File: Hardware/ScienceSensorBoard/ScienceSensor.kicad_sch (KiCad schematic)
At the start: 94 parts, among them J1 Conn_02x03_Counter_Clockwise, J2 RJ45_LED_Shielded, Q1 SI4156DY, Q10 BSS138, Q11 SI4156DY, Q2 SI4156DY, Q3 SI4156DY, Q4 BSS138, Q5 BSS138, Q6 BSS138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

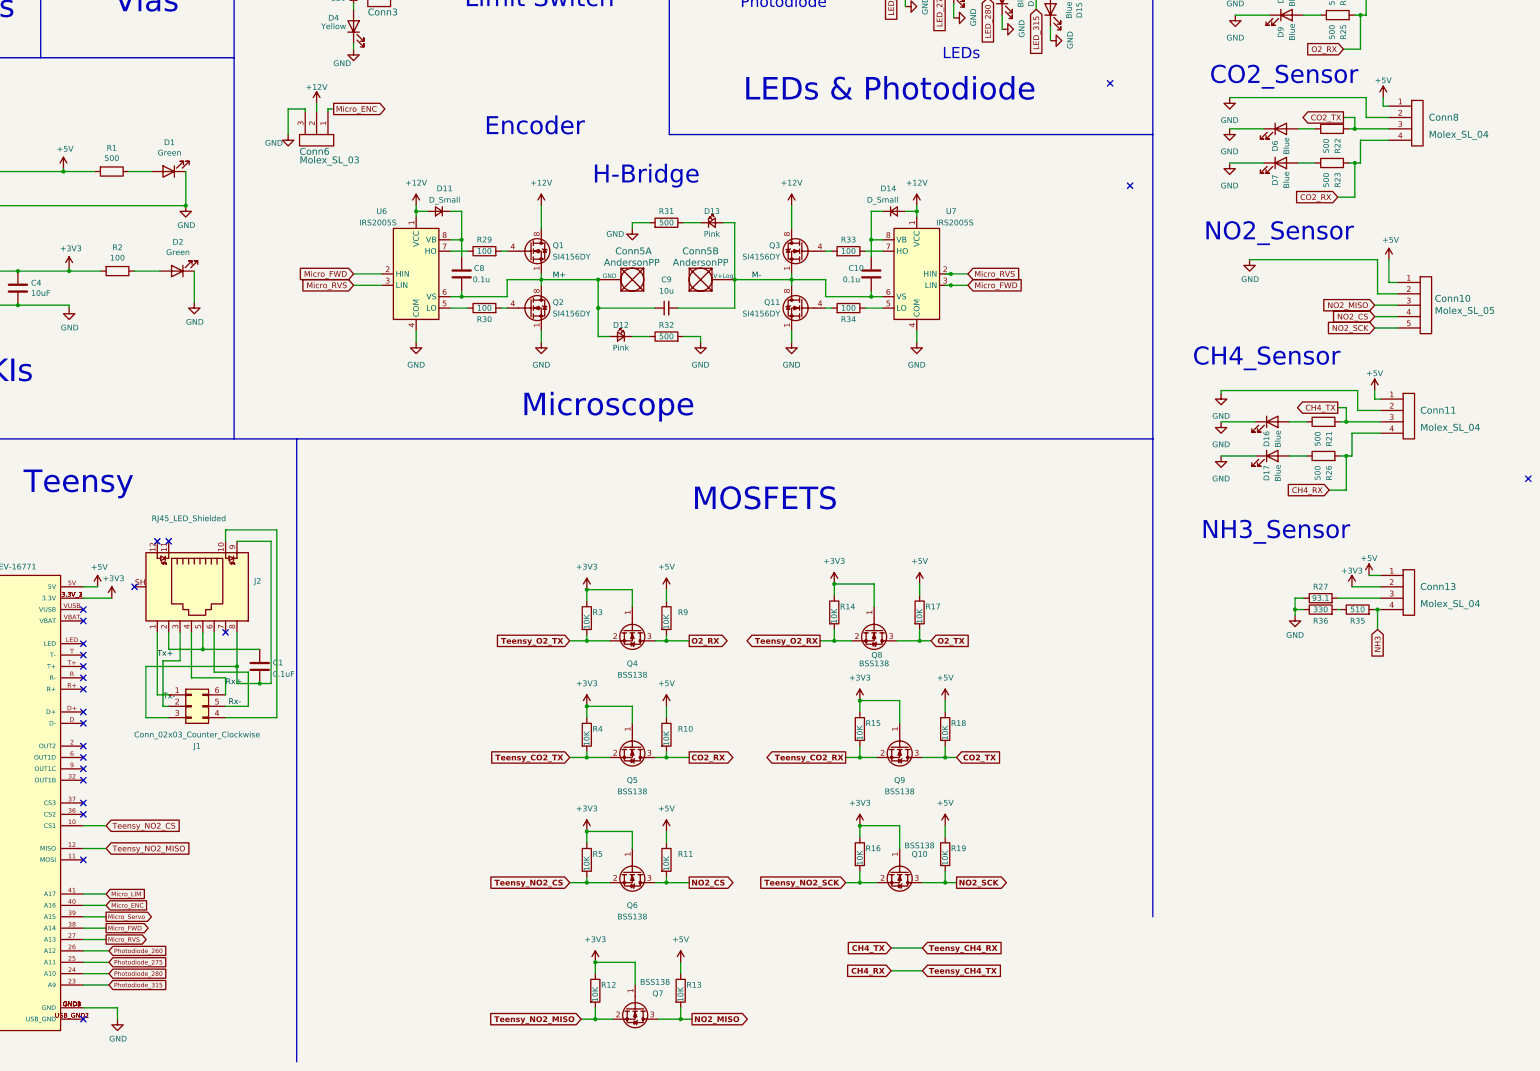
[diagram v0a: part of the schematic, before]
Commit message: ERC fixes
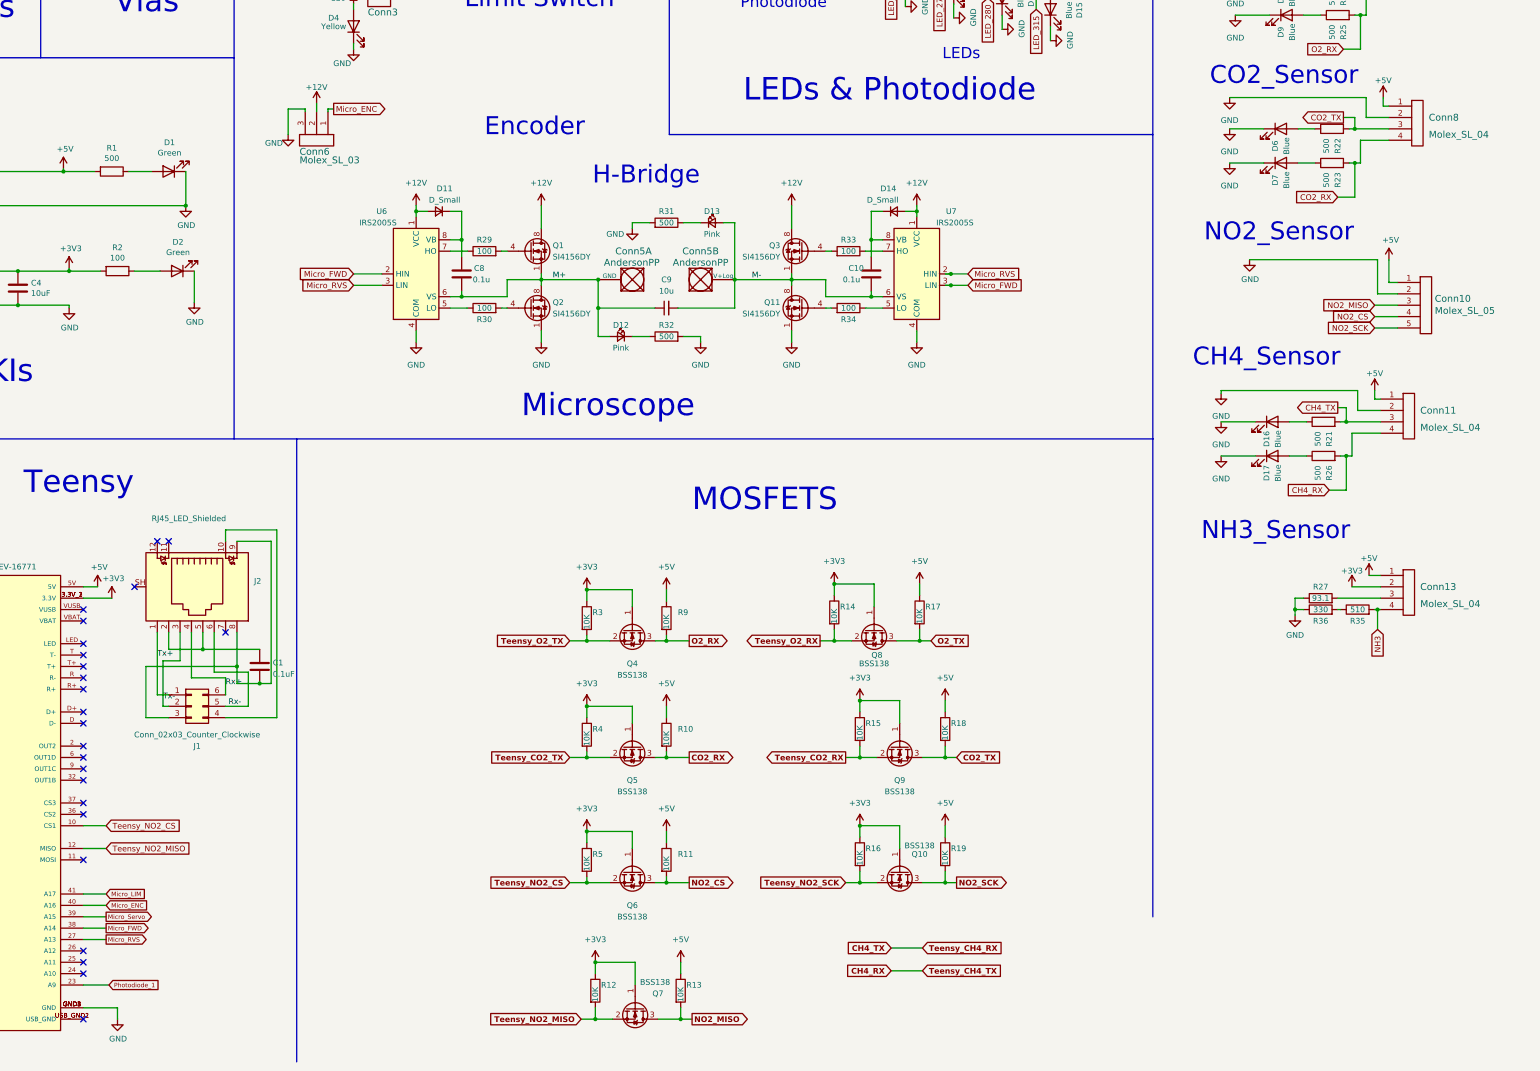
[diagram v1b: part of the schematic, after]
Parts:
- Conn10: footprint MRDT_Connectors:MOLEX_SL_05_Horizontal -> MRDT_Connectors:MOLEX_SL_05_Vertical
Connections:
- net Photodiode_315 is gone; now on net Photodiode_1: U3.23 (A9)
- net Photodiode_260: no longer names the net of U3.26 (A12)
- net Photodiode_275: no longer names the net of U3.25 (A11)
- net Photodiode_280: no longer names the net of U3.24 (A10)
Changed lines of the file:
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@@
   (no_connect (at 37.465 240.03))
   (no_connect (at 78.105 229.87))
+  (no_connect (at 78.105 260.35))
+  (no_connect (at 78.105 262.89))
+  (no_connect (at 78.105 265.43))
   (no_connect (at 94.615 168.91))
   (no_connect (at 97.155 168.91))
@@
   (no_connect (at 37.465 257.81))
   (no_connect (at 37.465 260.35))
-  (no_connect (at 400.685 154.94))
-  (no_connect (at 311.785 89.535))
-  (no_connect (at 307.34 66.675))
   (no_connect (at 297.18 24.765))
   (no_connect (at 37.465 234.95))
@@
     (stroke (width 0) (type default) (color 0 0 0 0))
   )
-  (wire (pts (xy 83.82 260.35) (xy 78.105 260.35))
-    (stroke (width 0) (type default) (color 0 0 0 0))
-  )
   (wire (pts (xy 172.72 110.49) (xy 180.34 110.49))
     (stroke (width 0) (type default) (color 0 0 0 0))
@@
     (stroke (width 0) (type default) (color 0 0 0 0))
   )
-  (wire (pts (xy 83.82 262.89) (xy 78.105 262.89))
-    (stroke (width 0) (type default) (color 0 0 0 0))
-  )
   (wire (pts (xy 33.655 212.09) (xy 37.465 212.09))
     (stroke (width 0) (type default) (color 0 0 0 0))
@@
     (stroke (width 0) (type default) (color 0 0 0 0))
   )
-  (wire (pts (xy 83.82 265.43) (xy 78.105 265.43))
-    (stroke (width 0) (type default) (color 0 0 0 0))
-  )
   (wire (pts (xy 270.51 204.47) (xy 270.51 207.01))
     (stroke (width 0) (type default) (color 0 0 0 0))
@@
     )
   )
-  (global_label "Photodiode_315" (shape input) (at 83.82 267.97 0) (fields_autoplaced)
+  (global_label "Photodiode_1" (shape input) (at 83.82 267.97 0) (fields_autoplaced)
     (effects (font (size 0.9906 0.9906)) (justify left))
-    (property "Intersheet References" "${INTERSHEET_REFS}" (id 0) (at 97.4727 267.9081 0)
+    (property "Intersheet References" "${INTERSHEET_REFS}" (id 0) (at 95.5859 267.9081 0)
       (effects (font (size 0.9906 0.9906)) (justify left) hide)
     )
@@
     )
   )
-  (global_label "Photodiode_280" (shape input) (at 83.82 265.43 0) (fields_autoplaced)
-    (effects (font (size 0.9906 0.9906)) (justify left))
-    (property "Intersheet References" "${INTERSHEET_REFS}" (id 0) (at 97.4727 265.3681 0)
-      (effects (font (size 0.9906 0.9906)) (justify left) hide)
-    )
-  )
   (global_label "Photodiode_1" (shape output) (at 226.06 42.545 180) (fields_autoplaced)
     (effects (font (size 1.27 1.27)) (justify right))
@@
     )
   )
-  (global_label "Photodiode_275" (shape input) (at 83.82 262.89 0) (fields_autoplaced)
-    (effects (font (size 0.9906 0.9906)) (justify left))
-    (property "Intersheet References" "${INTERSHEET_REFS}" (id 0) (at 97.4727 262.8281 0)
-      (effects (font (size 0.9906 0.9906)) (justify left) hide)
-    )
-  )
   (global_label "Micro_FWD" (shape output) (at 83.185 255.27 0) (fields_autoplaced)
     (effects (font (size 1 1)) (justify left))
@@
     )
   )
-  (global_label "Photodiode_260" (shape input) (at 83.82 260.35 0) (fields_autoplaced)
-    (effects (font (size 0.9906 0.9906)) (justify left))
-    (property "Intersheet References" "${INTERSHEET_REFS}" (id 0) (at 97.4727 260.2881 0)
-      (effects (font (size 0.9906 0.9906)) (justify left) hide)
-    )
-  )
   (global_label "NO2_MISO" (shape output) (at 213.995 275.59 0) (fields_autoplaced)
     (effects (font (size 1.27 1.27) bold) (justify left))
@@
       (effects (font (size 1.524 1.524)) (justify left))
     )
-    (property "Footprint" "MRDT_Connectors:MOLEX_SL_05_Horizontal" (id 2) (at 376.555 122.555 0)
+    (property "Footprint" "MRDT_Connectors:MOLEX_SL_05_Vertical" (id 2) (at 376.555 122.555 0)
       (effects (font (size 1.524 1.524)) hide)
     )
@@
     )
     (path "/c5c8c731-d752-4329-b481-00d81fff6183"
-      (reference "Conn10") (unit 1) (value "Molex_SL_05") (footprint "MRDT_Connectors:MOLEX_SL_05_Horizontal")
+      (reference "Conn10") (unit 1) (value "Molex_SL_05") (footprint "MRDT_Connectors:MOLEX_SL_05_Vertical")
     )
     (path "/2fc579ad-59f7-42ce-8923-2fdbb5dabf35"

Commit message: unsaved changes
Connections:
- net +3V3: no longer Conn13.2
- net +5V: now also Conn13.2
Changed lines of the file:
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@@
   (junction (at 245.745 178.435) (diameter 0) (color 0 0 0 0)
   )
+  (junction (at 365.125 176.53) (diameter 0) (color 0 0 0 0)
+  )
   (junction (at 367.03 184.15) (diameter 0) (color 0 0 0 0)
   )
@@
     (stroke (width 0) (type default) (color 0 0 0 0))
   )
+  (wire (pts (xy 365.125 179.07) (xy 367.665 179.07))
+    (stroke (width 0) (type default) (color 0 0 0 0))
+  )
   (wire (pts (xy 208.28 179.705) (xy 208.28 182.245))
     (stroke (width 0) (type default) (color 0 0 0 0))
@@
     (stroke (width 0) (type default) (color 0 0 0 0))
   )
-  (wire (pts (xy 361.315 179.07) (xy 367.665 179.07))
-    (stroke (width 0) (type default) (color 0 0 0 0))
-  )
   (wire (pts (xy 368.3 71.755) (xy 368.3 69.85))
     (stroke (width 0) (type default) (color 0 0 0 0))
@@
     (stroke (width 0) (type default) (color 0 0 0 0))
   )
+  (wire (pts (xy 365.125 176.53) (xy 365.125 179.07))
+    (stroke (width 0) (type default) (color 0 0 0 0))
+  )
   (wire (pts (xy 356.235 157.48) (xy 360.045 157.48))
     (stroke (width 0) (type default) (color 0 0 0 0))
@@
     (stroke (width 0) (type default) (color 0 0 0 0))
   )
+  (wire (pts (xy 363.855 176.53) (xy 365.125 176.53))
+    (stroke (width 0) (type default) (color 0 0 0 0))
+  )
   (polyline (pts (xy 316.865 146.05) (xy 316.865 252.73))
     (stroke (width 0) (type default) (color 0 0 0 0))
@@
     (pin "2")
   )
-  (symbol (lib_id "power:+3V3") (at 361.315 179.07 0) (unit 1)
-    (in_bom yes) (on_board yes) (fields_autoplaced)
-    (property "Reference" "#PWR043" (id 0) (at 361.315 182.88 0)
-      (effects (font (size 1.27 1.27)) hide)
-    )
-    (property "Value" "+3V3" (id 1) (at 361.315 175.4942 0))
-    (property "Footprint" "" (id 2) (at 361.315 179.07 0)
-      (effects (font (size 1.27 1.27)) hide)
-    )
-    (property "Datasheet" "" (id 3) (at 361.315 179.07 0)
-      (effects (font (size 1.27 1.27)) hide)
-    )
-    (pin "1")
-  )
   (symbol (lib_id "power:GND") (at 338.455 106.045 0) (unit 1)
     (in_bom yes) (on_board yes)
@@
     (pin "1")
   )
-  (symbol (lib_id "power:+5V") (at 365.125 176.53 0) (unit 1)
+  (symbol (lib_id "power:+5V") (at 363.855 176.53 0) (unit 1)
     (in_bom yes) (on_board yes)
-    (property "Reference" "#PWR032" (id 0) (at 365.125 180.34 0)
+    (property "Reference" "#PWR032" (id 0) (at 363.855 180.34 0)
       (effects (font (size 1.27 1.27)) hide)
     )
-    (property "Value" "+5V" (id 1) (at 365.125 172.72 0))
-    (property "Footprint" "" (id 2) (at 365.125 176.53 0)
+    (property "Value" "+5V" (id 1) (at 363.855 172.72 0))
+    (property "Footprint" "" (id 2) (at 363.855 176.53 0)
       (effects (font (size 1.27 1.27)) hide)
     )
-    (property "Datasheet" "" (id 3) (at 365.125 176.53 0)
+    (property "Datasheet" "" (id 3) (at 363.855 176.53 0)
       (effects (font (size 1.27 1.27)) hide)
     )
@@
       (reference "#PWR042") (unit 1) (value "+5V") (footprint "")
     )
-    (path "/a654e81f-761e-4b11-90f6-0efc0dc296c1"
-      (reference "#PWR043") (unit 1) (value "+3V3") (footprint "")
-    )
     (path "/6a1ff8e3-c079-48e3-86f8-a888ae7895ea"

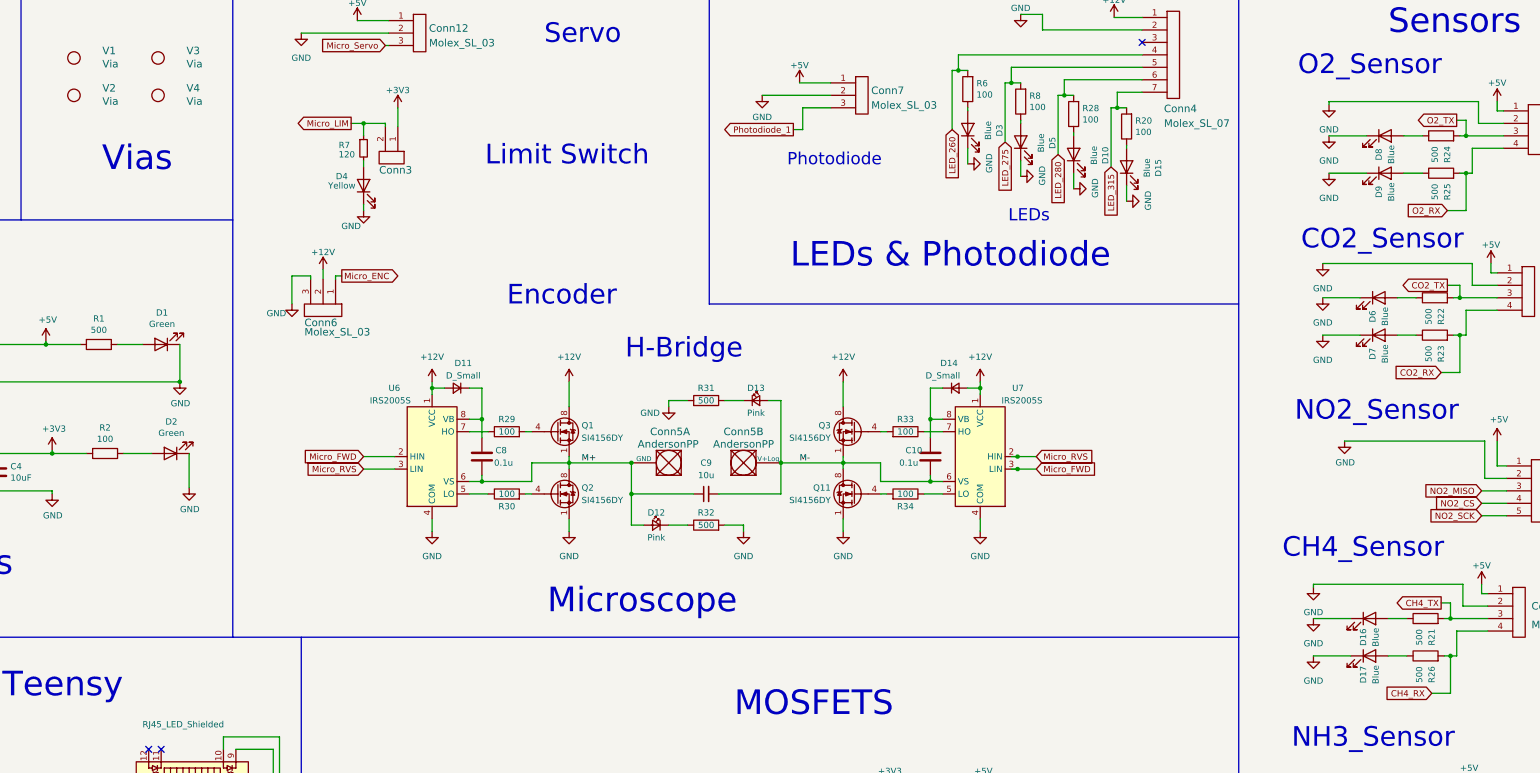
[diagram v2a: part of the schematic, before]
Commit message: Resistor Values 100>120 & 500>330
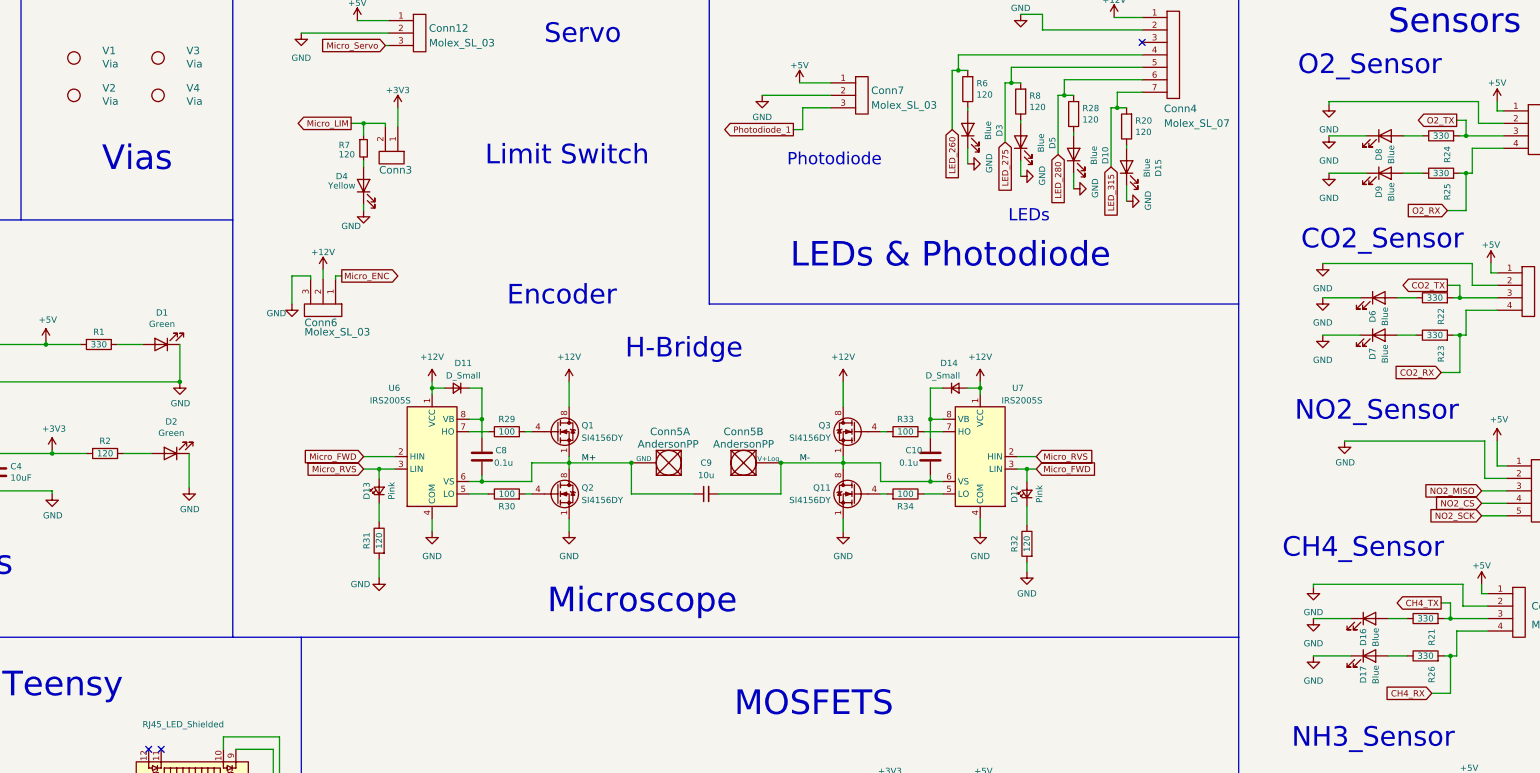
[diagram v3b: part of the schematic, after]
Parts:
- R1, R21, R22, R23, R24, R25, R26: value 500 -> 330
- R2, R20, R28, R6, R8: value 100 -> 120
- R31, R32: value 500 -> 120
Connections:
- net M+: no longer D12.2 (A)
- net M-: no longer D13.2 (A)
- net Micro_FWD: now also D12.2 (A)
- net Micro_RVS: now also D13.2 (A)
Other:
- moved on the sheet: D12, D13, R31, R32
